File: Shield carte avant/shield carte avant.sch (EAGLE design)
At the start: 23 parts, among them IC1 MCP2562-E_P, IC2 MCP2515-I_P, J1 22-05-7078-07, J2 22-05-7028-02, J3 22-05-7038-03, J5 22-05-7028-02, M1 ARDUINO_R3_ICSP

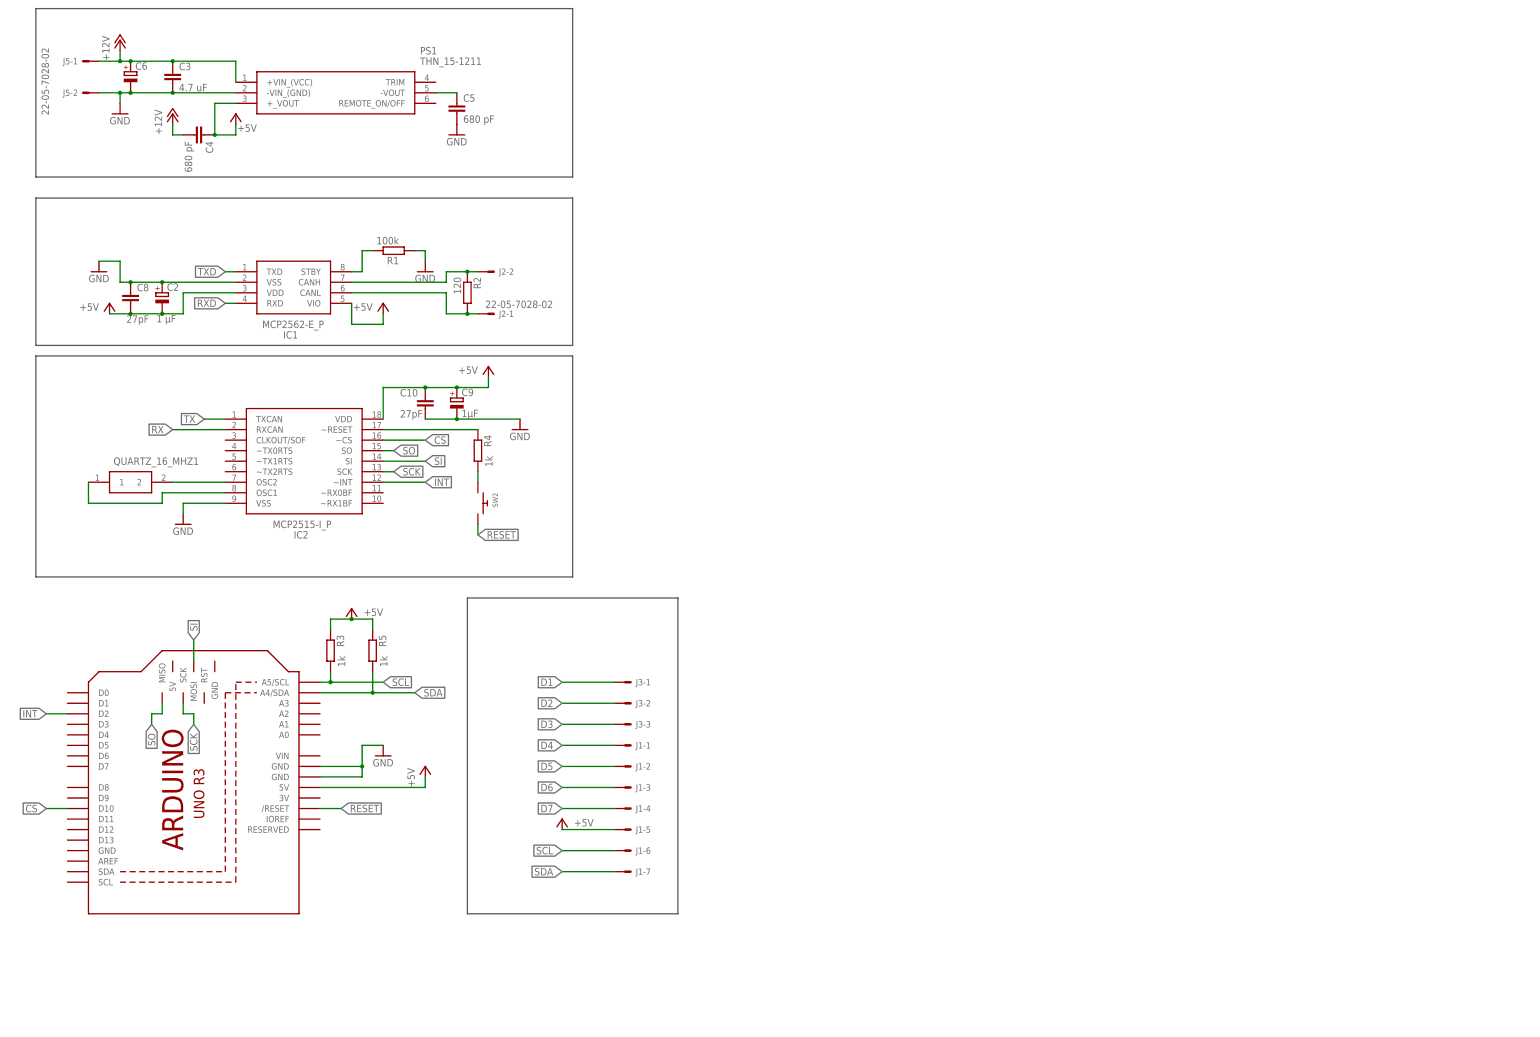
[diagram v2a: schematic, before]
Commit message: Début ajout relais pour les boutons lumineux
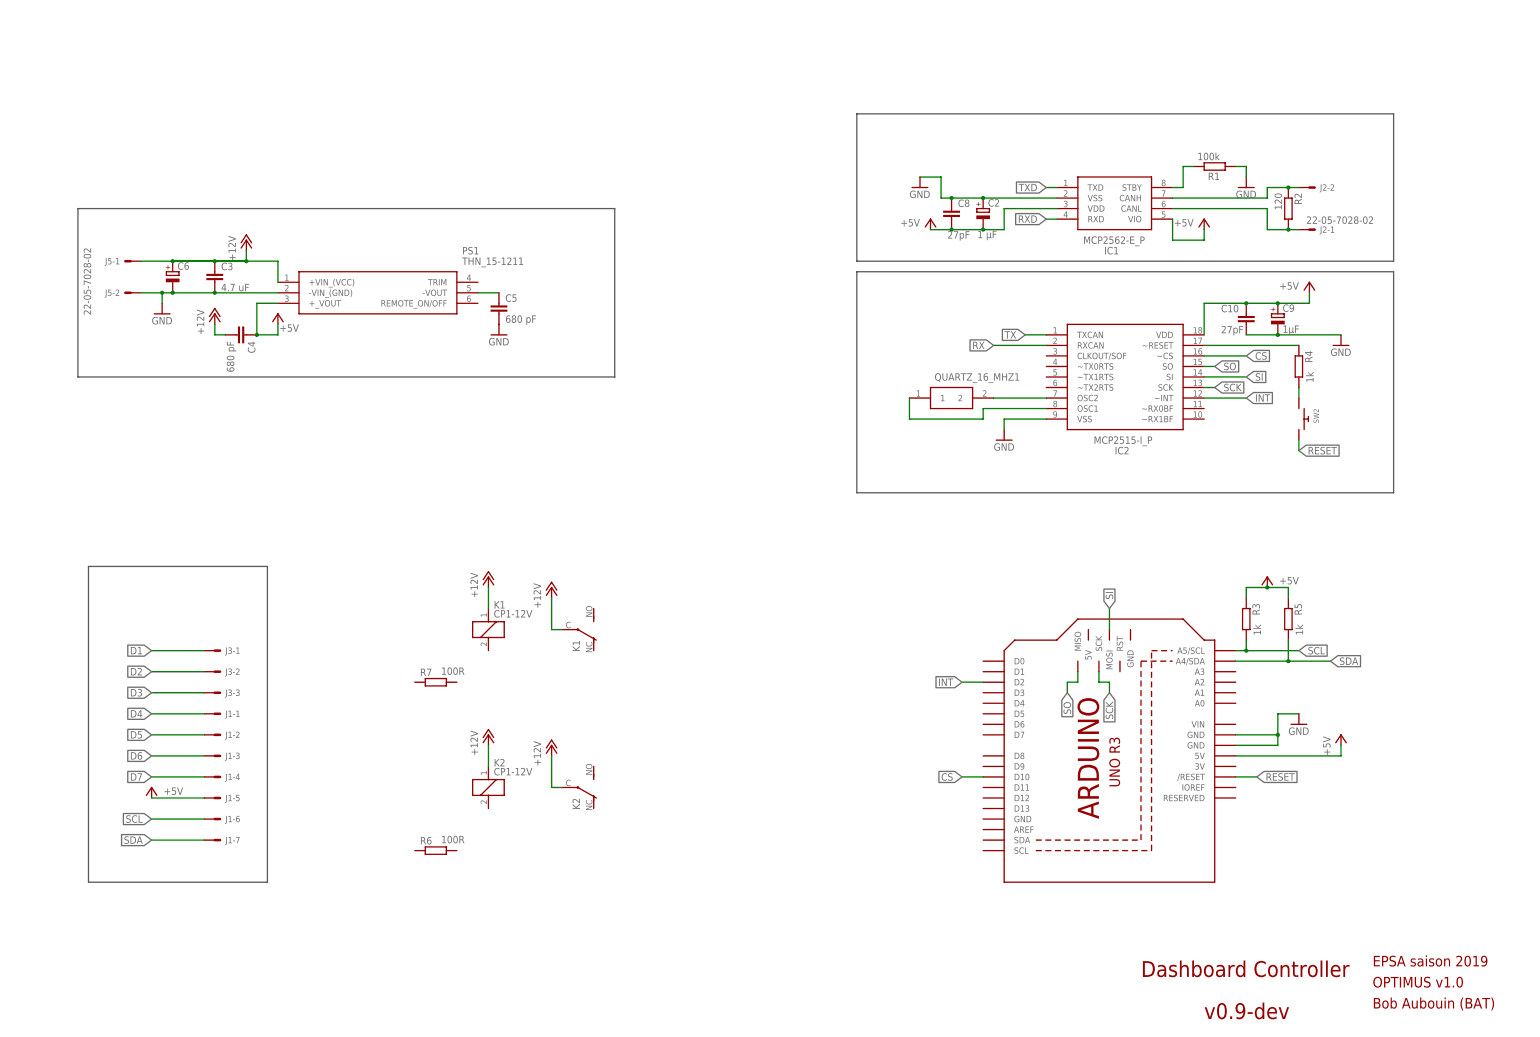
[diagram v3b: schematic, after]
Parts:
- added K1, K2: CP1-12V, relay:CP1-12V
- added R6, R7: 100R, rcl:R-EU_0204/7
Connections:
- net +12V: now also K11.1, K12.P, K21.1, K22.P
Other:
- note added: "Bob Aubouin (BAT)"
- note added: "Dashboard Controller"
- note added: "EPSA saison 2019"
- note added: "OPTIMUS v1.0"
- note added: "v0.9-dev"
- moved on the sheet: C10, C2, C3, C4, C5, C6, C8, C9, IC1, IC2, J1-1, J1-2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

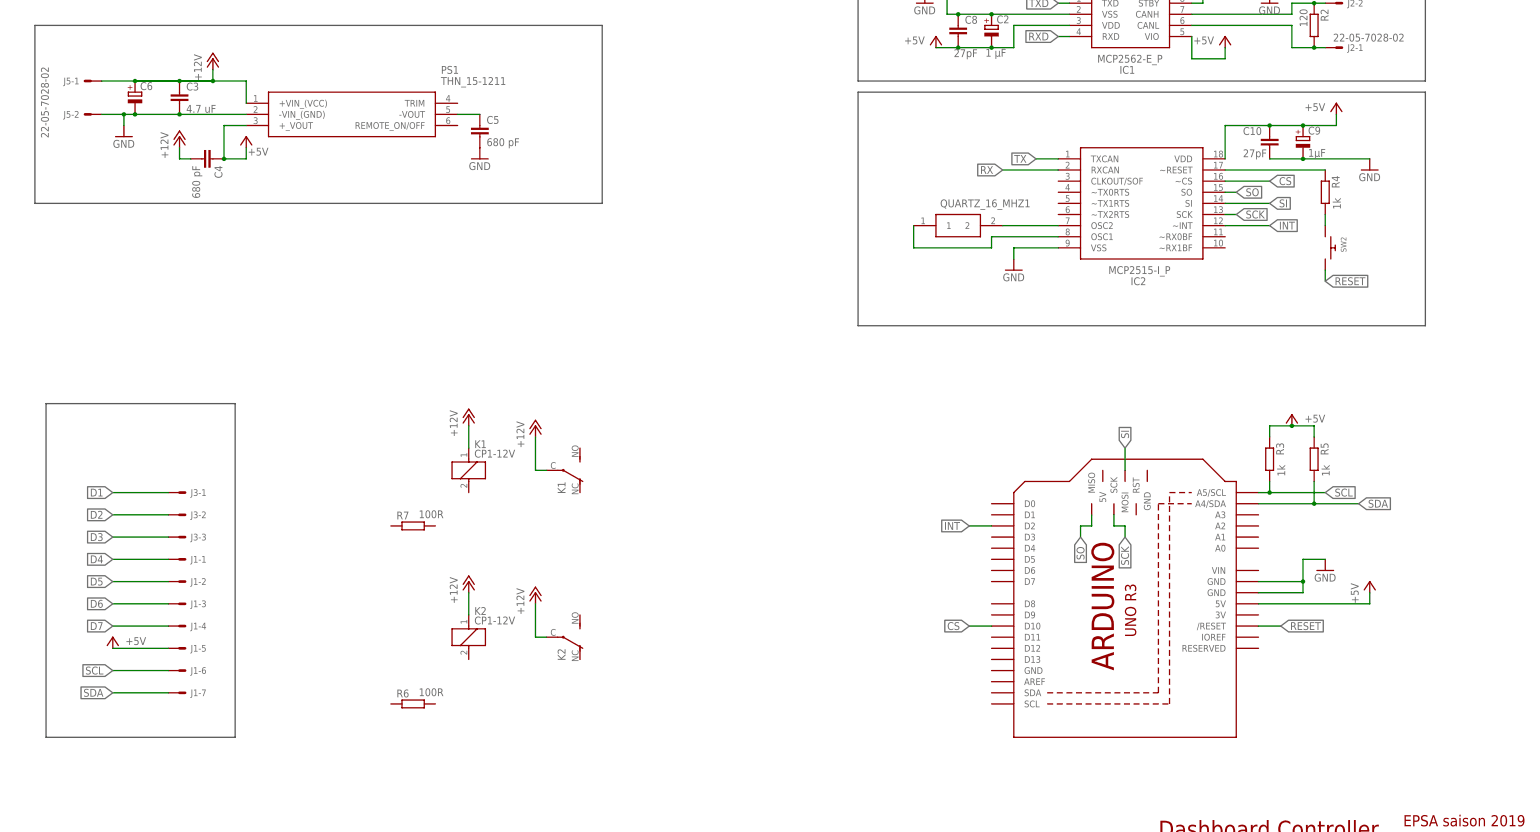
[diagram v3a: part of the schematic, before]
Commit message: Ajout des MOSFET pour gérer l'affichage des boutons
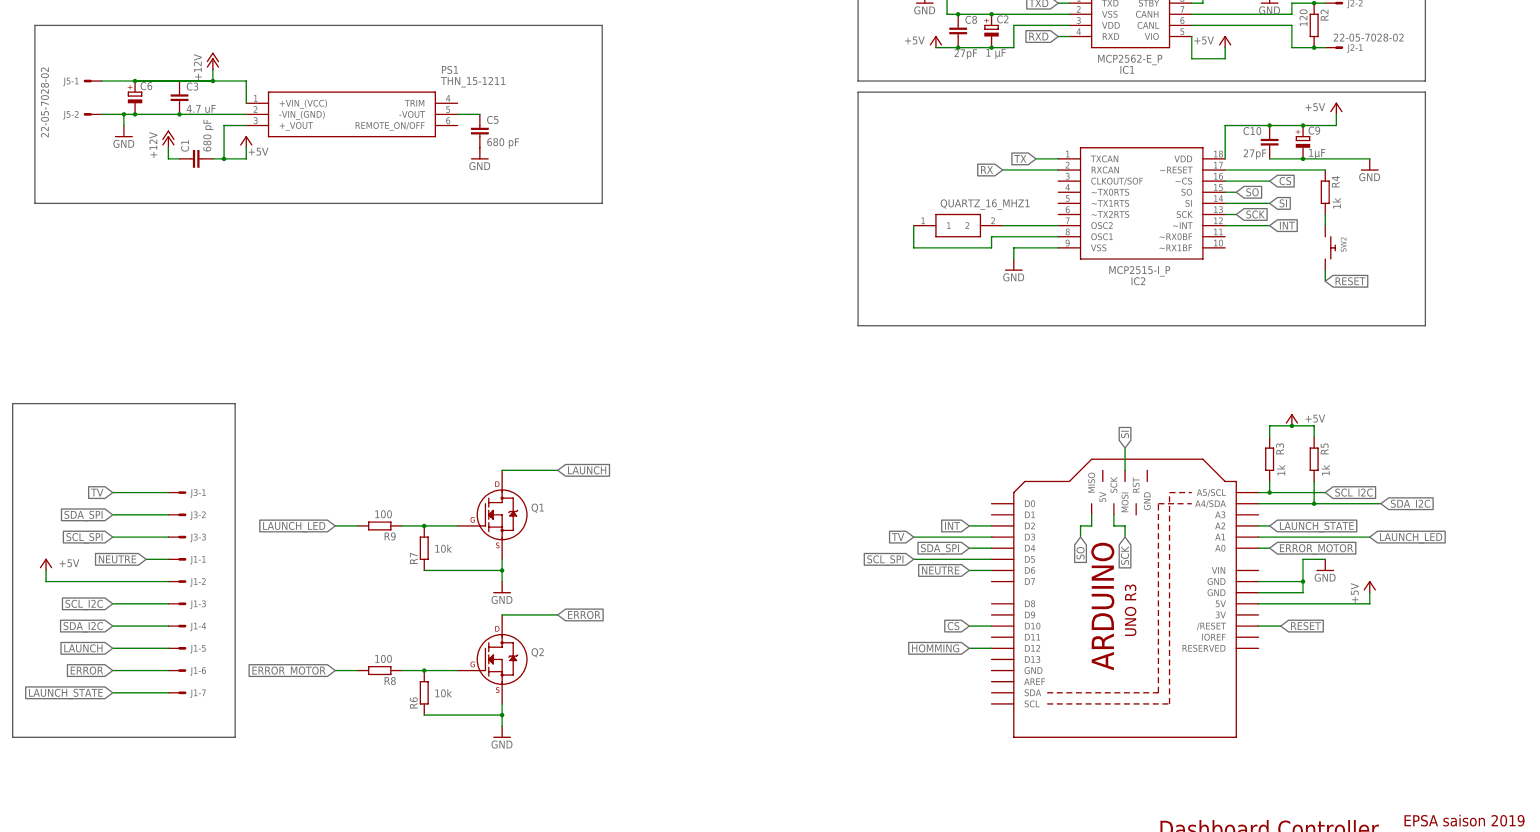
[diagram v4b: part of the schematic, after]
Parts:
- removed C4: 680 pF, rcl:C-EU025-024X044
- removed K1, K2: CP1-12V, relay:CP1-12V
- added C1: 680 pF, rcl:C-EU025-024X044
- added Q1, Q2: (no value), transistors:2N7000_TO92
- added R8, R9: 100, rcl:R-EU_0204/7
- R6, R7: value 100R -> 10k
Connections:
- removed net D1: J3-1.S
- removed net D2: J3-2.S
- removed net D3: J3-3.S
- removed net D4: J1-1.S
- removed net D5: J1-2.S
- removed net D6: J1-3.S
- removed net D7: J1-4.S
- removed net SCL: J1-6.S, M1.A5/SCL, R3.2
- removed net SDA: J1-7.S, M1.A4/SDA, R5.2
- new net ERROR: J1-6.S, Q2.D
- new net ERROR_MOTOR: M1.A0, R8.2
- new net HOMMING: M1.D12
- new net LAUNCH: J1-5.S, Q1.D
- new net LAUNCH_LED: M1.A1, R9.2
- new net LAUNCH_STATE: J1-7.S, M1.A2
- new net N$12: Q2.G, R6.2, R8.1
- new net N$13: Q1.G, R7.2, R9.1
- new net NEUTRE: J1-1.S, M1.D6
- new net SCL_I2C: J1-3.S, M1.A5/SCL, R3.2
- new net SCL_SPI: J3-3.S, M1.D5
- new net SDA_I2C: J1-4.S, M1.A4/SDA, R5.2
- new net SDA_SPI: J3-2.S, M1.D4
- new net TV: J3-1.S, M1.D3
- net +12V: now also C1.1; no longer C4.2, K11.1, K12.P, K21.1, K22.P
- net +5V: now also C1.2, J1-2.S; no longer C4.1, J1-5.S
- net GND: now also Q1.S, Q2.S, R6.1, R7.1
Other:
- moved on the sheet: R6, R7

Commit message: Fin du routage et vérification sérigraphie
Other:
- note added: "5V vers 12V pour boutons lumineux"
- moved on the sheet: C1, C3, C5, C6, J1-1, J1-2, J1-3, J1-4, J1-5, J1-6, J1-7, J3-1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

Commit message: Sérigraphie
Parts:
- C3: value 4.7 uF -> 27 pF
- C6: value (none) -> 1 µF
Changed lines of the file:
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@@
 <part name="GND5" library="supply1" deviceset="GND" device=""/>
 <part name="PS1" library="THN_15-1211" deviceset="THN_15-1211" device=""/>
-<part name="C3" library="rcl" library_urn="urn:adsk.eagle:library:334" deviceset="C-EU" device="025-024X044" package3d_urn="urn:adsk.eagle:package:23630/1" value="4.7 uF"/>
+<part name="C3" library="rcl" library_urn="urn:adsk.eagle:library:334" deviceset="C-EU" device="025-024X044" package3d_urn="urn:adsk.eagle:package:23630/1" value="27 pF"/>
 <part name="C5" library="rcl" library_urn="urn:adsk.eagle:library:334" deviceset="C-EU" device="025-024X044" package3d_urn="urn:adsk.eagle:package:23630/1" value="680 pF"/>
 <part name="J2" library="con-molex" library_urn="urn:adsk.eagle:library:165" deviceset="22-?-02" device="05-7028"/>
@@
 <part name="GND8" library="supply1" deviceset="GND" device=""/>
 <part name="C2" library="rcl" library_urn="urn:adsk.eagle:library:334" deviceset="CPOL-EU" device="B45181A" package3d_urn="urn:adsk.eagle:package:23316/1" value="1 µF"/>
-<part name="C6" library="rcl" library_urn="urn:adsk.eagle:library:334" deviceset="CPOL-EU" device="B45181A" package3d_urn="urn:adsk.eagle:package:23316/1"/>
+<part name="C6" library="rcl" library_urn="urn:adsk.eagle:library:334" deviceset="CPOL-EU" device="B45181A" package3d_urn="urn:adsk.eagle:package:23316/1" value="1 µF"/>
 <part name="C8" library="rcl" library_urn="urn:adsk.eagle:library:334" deviceset="C-EU" device="025-030X050" package3d_urn="urn:adsk.eagle:package:23631/1" value="27pF"/>
 <part name="IC2" library="MCP2515-I_P" deviceset="MCP2515-I_P" device=""/>

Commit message: Revue PJR
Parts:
- removed C1: 680 pF, rcl:C-EU025-024X044
- added C7: 27pF, rcl:C-EU025-030X050
- C5: value 680 pF -> 27pF; device rcl:C-EU025-024X044 -> rcl:C-EU025-030X050
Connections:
- removed net N$2: R4.2, SW2.P$1
- removed net N$6: IC2.OSC2, QUARTZ_16_MHZ1.2
- removed net RX: IC2.RXCAN
- removed net TX: IC2.TXCAN
- net +12V: no longer C1.1
- net +5V: no longer C1.2
- net GND: now also C7.1, PS1.-VOUT, SW2.P$2
- net N$3: now also IC2.OSC1, QUARTZ_16_MHZ1.1; no longer PS1.-VOUT
- net N$7: now also C7.2, IC2.OSC2, QUARTZ_16_MHZ1.2; no longer IC2.OSC1, QUARTZ_16_MHZ1.1
- net RESET: now also R4.2, SW2.P$1; no longer SW2.P$2
- net RXD: now also IC2.RXCAN
- net TXD: now also IC2.TXCAN
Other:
- moved on the sheet: C5, QUARTZ_16_MHZ1

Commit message: maj numéro de version pour release
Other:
- note added: "v0.9"
- note removed: "v0.9-dev"
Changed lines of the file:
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@@
 <wire x1="350.52" y1="187.96" x2="220.98" y2="187.96" width="0.1524" layer="97"/>
 <text x="289.56" y="17.78" size="3.81" layer="94">Dashboard Controller</text>
-<text x="304.8" y="7.62" size="3.81" layer="94">v0.9-dev</text>
+<text x="304.8" y="7.62" size="3.81" layer="94">v0.9</text>
 <text x="345.44" y="20.32" size="2.54" layer="94">EPSA saison 2019</text>
 <text x="345.44" y="15.24" size="2.54" layer="94">OPTIMUS v1.0</text>
